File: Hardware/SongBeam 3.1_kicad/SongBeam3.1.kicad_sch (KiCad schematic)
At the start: 67 parts, among them IC1 ADAU7002ACBZ-R7, IC2 TXU0304PWR, IC3 TPS62842DGRR, IC4 TXU0304PWR, IC5 ADAU7002ACBZ-R7, IC6 LP5907MFX-1.8_NOPB, IC7 TEENSY_4.1, J1 Conn_01x02, J2 Conn_01x02, J3 Conn_01x04, J4 Conn_01x08, Q1 CPH6350-TL-W, Q2 AO6604, U1 TPL5110, U2 3034

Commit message: daughterBRD-UPDATE main BRD
added a full desing for daugther BRD, has a new microcontroller for 8 mics with TDM output
Start changes in the 4.0 version of the Soundbeam, making combatible with the daughter board
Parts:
- added C20, C21, C22: 22uF, Adafruit bq25185 Breakout:0805-NO, symbol Adafruit bq25185 Breakout-eagle-import:CAP_CERAMIC0805-NOOUTLINE
- added CHG0: ORANGE, Adafruit bq25185 Breakout:CHIPLED_0805_NOOUTLINE, symbol Adafruit bq25185 Breakout-eagle-import:LED0805_NOOUTLINE
- added D2 (x2): MBRX120, Adafruit bq25185 Breakout:SOD-123FL, symbol Adafruit bq25185 Breakout-eagle-import:DIODE-SCHOTTKYSOD-123FL
- added FAULT0: RED, Adafruit bq25185 Breakout:CHIPLED_0805_NOOUTLINE, symbol Adafruit bq25185 Breakout-eagle-import:LED0805_NOOUTLINE
- added IC8: BQ25185, Adafruit bq25185 Breakout:WSON10, symbol Adafruit bq25185 Breakout-eagle-import:BQ25185
- added JP2: HEADER-1X6OVALWAVE, Adafruit bq25185 Breakout:1X06_OVALWAVE, symbol Adafruit bq25185 Breakout-eagle-import:HEADER-1X6OVALWAVE
- added JP2, JP4: FIDUCIAL1.5X3, Adafruit bq25185 Breakout:FIDUCIAL_0.5MM, symbol Adafruit bq25185 Breakout-eagle-import:FIDUCIAL_0.5MM
- added JP7: HEADER-1X676MIL, Adafruit bq25185 Breakout:1X06_ROUND_76, symbol Adafruit bq25185 Breakout-eagle-import:HEADER-1X676MIL
- added R19, R21, R30: 5.1K, Adafruit bq25185 Breakout:0603-NO, symbol Adafruit bq25185 Breakout-eagle-import:RESISTOR_0603_NOOUT
- added R22, R23, R24: 1K, Adafruit bq25185 Breakout:0603-NO, symbol Adafruit bq25185 Breakout-eagle-import:RESISTOR_0603_NOOUT
- added R25, R31: 10K, Adafruit bq25185 Breakout:0603-NO, symbol Adafruit bq25185 Breakout-eagle-import:RESISTOR_0603_NOOUT
- added R26: 600, Adafruit bq25185 Breakout:0603-NO, symbol Adafruit bq25185 Breakout-eagle-import:RESISTOR_0603_NOOUT
- added R27: 300, Adafruit bq25185 Breakout:0603-NO, symbol Adafruit bq25185 Breakout-eagle-import:RESISTOR_0603_NOOUT
- added R28: 13K, Adafruit bq25185 Breakout:0603-NO, symbol Adafruit bq25185 Breakout-eagle-import:RESISTOR_0603_NOOUT
- added R29: 1200, Adafruit bq25185 Breakout:0603-NO, symbol Adafruit bq25185 Breakout-eagle-import:RESISTOR_0603_NOOUT
- added SJ1, SJ2, SJ3: SOLDERJUMPER_CLOSED, Adafruit bq25185 Breakout:SOLDERJUMPER_CLOSEDWIRE, symbol Adafruit bq25185 Breakout-eagle-import:SOLDERJUMPER_CLOSED
- added SJ4, SJ5, SJ6: SOLDERJUMPER, Adafruit bq25185 Breakout:SOLDERJUMPER_ARROW_NOPASTE, symbol Adafruit bq25185 Breakout-eagle-import:SOLDERJUMPER
- added U$11, U$16, U$18, U$19: MOUNTINGHOLE2.5, Adafruit bq25185 Breakout:MOUNTINGHOLE_2.5_PLATED, symbol Adafruit bq25185 Breakout-eagle-import:MOUNTINGHOLE2.5
- added VBAT0, VSYS0: JST2PH, Adafruit bq25185 Breakout:JSTPH2_BATT, symbol Adafruit bq25185 Breakout-eagle-import:CON_JST_PH_2PIN_MT_BATT
- added VSYSOK0: GREEN, Adafruit bq25185 Breakout:CHIPLED_0805_NOOUTLINE, symbol Adafruit bq25185 Breakout-eagle-import:LED0805_NOOUTLINE
- added X3: USBC, Adafruit bq25185 Breakout:USB_C_CUSB31-CFM2AX-01-X, symbol Adafruit bq25185 Breakout-eagle-import:USB_C
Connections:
- net GND: now also C20.2, C21.2, C22.2, IC8.5 (GND), IC8.PAD (GND), JP2.1, JP2.3, JP2.5, R19.1, R21.1, R22.2, R25.1, R26.2, R28.2, R31.1, SJ4.1, SJ5.1, SJ6.1, VBAT0.1, VBAT0.NC1 (P$1), VBAT0.NC2 (P$1), VSYS0.1, VSYS0.NC1 (P$1), VSYS0.NC2 (P$1), X3.A1B12 (GND), X3.B1A12 (GND)
- new net: R28.1, SJ2.1
- new net: D2.A, JP2.2
- new net: R22.1, VSYSOK0.C
- new net: R31.2, SJ1.1
- new net: CHG0.C, R23.2
- new net: R30.2, SJ6.2
- new net: FAULT0.C, R24.2
- new net: R19.2, X3.B5 (CC2)
- new net: R21.2, X3.A5 (CC1)
- new net: R27.2, SJ4.2
- new net: R26.1, SJ3.2
- new net: R29.2, SJ5.2
- new net: X3.A6 (D+), X3.B6 (D+)
- new net: X3.A7 (D-), X3.B7 (D-)
- new net /CE: IC8.4 (/CE), JP7.6, R25.2
- new net 5.0V: C21.1, CHG0.A, FAULT0.A, IC8.1 (VSYS), JP2.4, VSYS0.2, VSYSOK0.A
- new net ISET: IC8.8 (ISET), JP7.3, R27.1, R29.1, SJ3.1
- new net STAT1: IC8.9 (STAT1), JP7.4, R24.1
- new net STAT2: IC8.3 (STAT2), JP7.5, R23.1
- new net THERM: IC8.6 (TS/MR), JP7.1, SJ1.2
- new net USB: D2.A, X3.A4B9 (VBUS), X3.B4A9 (VBUS)
- new net VBAT: C22.1, IC8.2 (VBAT), JP2.6, VBAT0.2
- new net VBUS: C20.1, D2.C, D2.C, IC8.10 (VBUS)
- new net VSET: IC8.7 (VSET), JP7.2, R30.1, SJ2.2
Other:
- note added: "300Ω = 1000mA 600Ω = 500mA 1200Ω = 250mA"
- note added: "5.1KΩ = 3.65V / 1A 12KΩ = 4.2V / 1A"

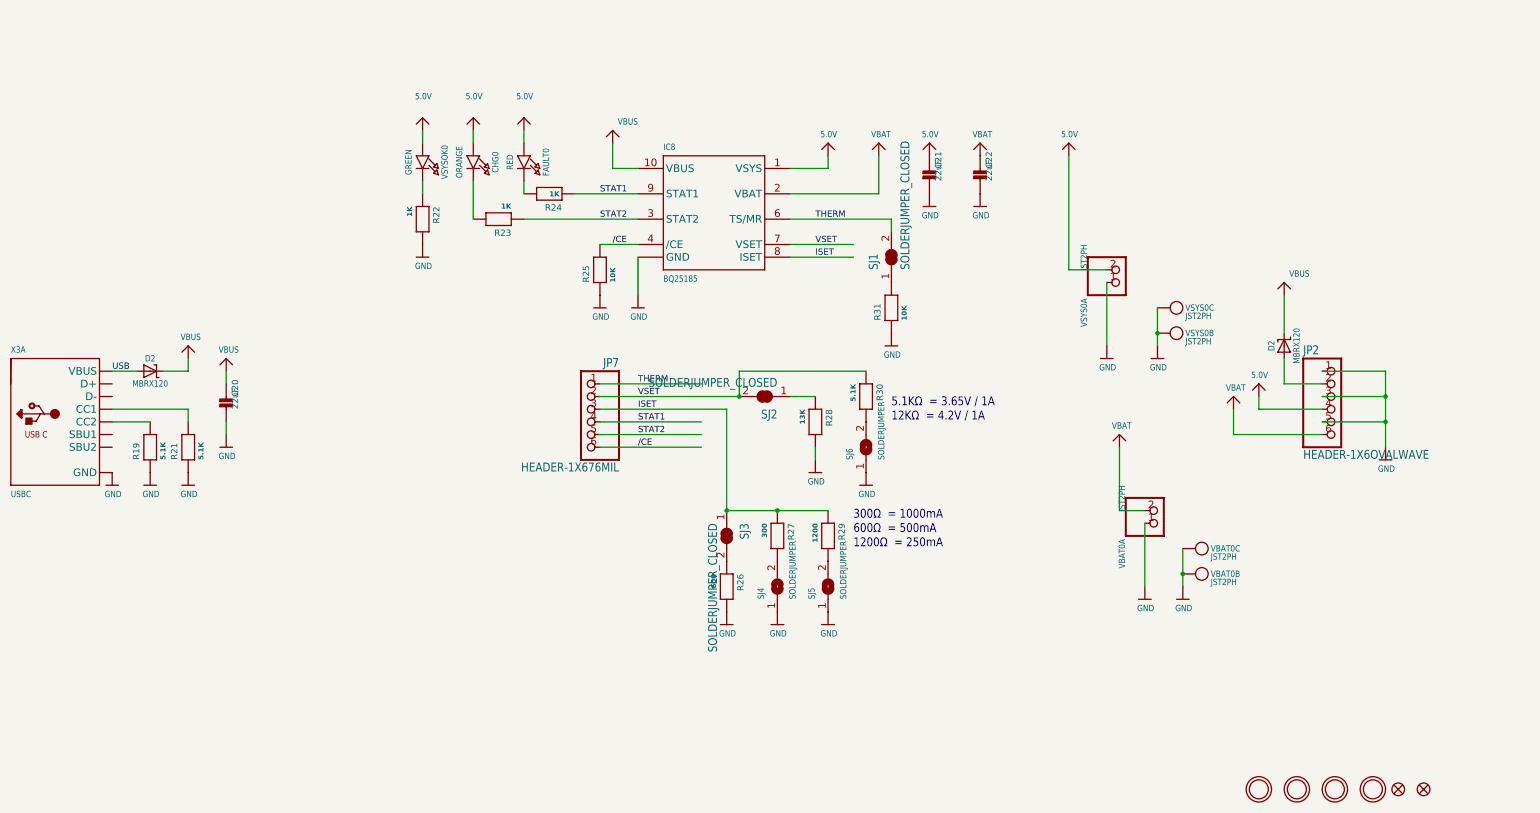
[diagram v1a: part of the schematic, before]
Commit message: tweaks in daugtherboard and develop in the main 4.0 board
changed voltage, added voltage translators and swiched from ethernet to HDMI
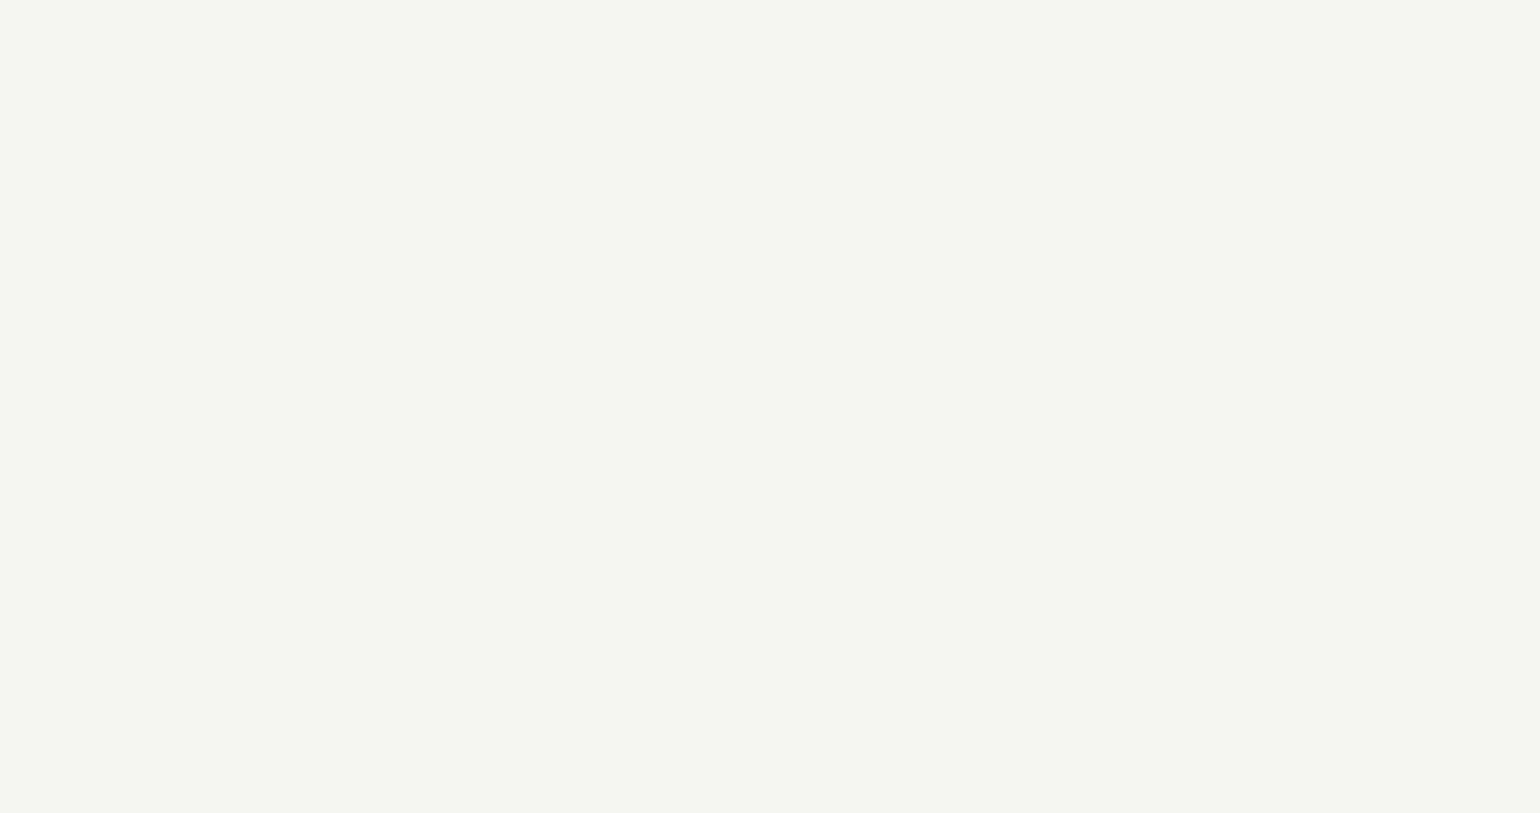
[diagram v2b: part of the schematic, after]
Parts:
- removed C20, C21, C22: 22uF, Adafruit bq25185 Breakout:0805-NO, symbol Adafruit bq25185 Breakout-eagle-import:CAP_CERAMIC0805-NOOUTLINE
- removed CHG0: ORANGE, Adafruit bq25185 Breakout:CHIPLED_0805_NOOUTLINE, symbol Adafruit bq25185 Breakout-eagle-import:LED0805_NOOUTLINE
- removed D2 (x2): MBRX120, Adafruit bq25185 Breakout:SOD-123FL, symbol Adafruit bq25185 Breakout-eagle-import:DIODE-SCHOTTKYSOD-123FL
- removed FAULT0: RED, Adafruit bq25185 Breakout:CHIPLED_0805_NOOUTLINE, symbol Adafruit bq25185 Breakout-eagle-import:LED0805_NOOUTLINE
- removed IC8: BQ25185, Adafruit bq25185 Breakout:WSON10, symbol Adafruit bq25185 Breakout-eagle-import:BQ25185
- removed JP2: HEADER-1X6OVALWAVE, Adafruit bq25185 Breakout:1X06_OVALWAVE, symbol Adafruit bq25185 Breakout-eagle-import:HEADER-1X6OVALWAVE
- removed JP2, JP4: FIDUCIAL1.5X3, Adafruit bq25185 Breakout:FIDUCIAL_0.5MM, symbol Adafruit bq25185 Breakout-eagle-import:FIDUCIAL_0.5MM
- removed JP7: HEADER-1X676MIL, Adafruit bq25185 Breakout:1X06_ROUND_76, symbol Adafruit bq25185 Breakout-eagle-import:HEADER-1X676MIL
- removed R19, R21, R30: 5.1K, Adafruit bq25185 Breakout:0603-NO, symbol Adafruit bq25185 Breakout-eagle-import:RESISTOR_0603_NOOUT
- removed R22, R23, R24: 1K, Adafruit bq25185 Breakout:0603-NO, symbol Adafruit bq25185 Breakout-eagle-import:RESISTOR_0603_NOOUT
- removed R25, R31: 10K, Adafruit bq25185 Breakout:0603-NO, symbol Adafruit bq25185 Breakout-eagle-import:RESISTOR_0603_NOOUT
- removed R26: 600, Adafruit bq25185 Breakout:0603-NO, symbol Adafruit bq25185 Breakout-eagle-import:RESISTOR_0603_NOOUT
- removed R27: 300, Adafruit bq25185 Breakout:0603-NO, symbol Adafruit bq25185 Breakout-eagle-import:RESISTOR_0603_NOOUT
- removed R28: 13K, Adafruit bq25185 Breakout:0603-NO, symbol Adafruit bq25185 Breakout-eagle-import:RESISTOR_0603_NOOUT
- removed R29: 1200, Adafruit bq25185 Breakout:0603-NO, symbol Adafruit bq25185 Breakout-eagle-import:RESISTOR_0603_NOOUT
- removed SJ1, SJ2, SJ3: SOLDERJUMPER_CLOSED, Adafruit bq25185 Breakout:SOLDERJUMPER_CLOSEDWIRE, symbol Adafruit bq25185 Breakout-eagle-import:SOLDERJUMPER_CLOSED
- removed SJ4, SJ5, SJ6: SOLDERJUMPER, Adafruit bq25185 Breakout:SOLDERJUMPER_ARROW_NOPASTE, symbol Adafruit bq25185 Breakout-eagle-import:SOLDERJUMPER
- removed U$11, U$16, U$18, U$19: MOUNTINGHOLE2.5, Adafruit bq25185 Breakout:MOUNTINGHOLE_2.5_PLATED, symbol Adafruit bq25185 Breakout-eagle-import:MOUNTINGHOLE2.5
- removed VBAT0, VSYS0: JST2PH, Adafruit bq25185 Breakout:JSTPH2_BATT, symbol Adafruit bq25185 Breakout-eagle-import:CON_JST_PH_2PIN_MT_BATT
- removed VSYSOK0: GREEN, Adafruit bq25185 Breakout:CHIPLED_0805_NOOUTLINE, symbol Adafruit bq25185 Breakout-eagle-import:LED0805_NOOUTLINE
- removed X3: USBC, Adafruit bq25185 Breakout:USB_C_CUSB31-CFM2AX-01-X, symbol Adafruit bq25185 Breakout-eagle-import:USB_C
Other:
- note removed: "300Ω = 1000mA 600Ω = 500mA 1200Ω = 250mA"
- note removed: "5.1KΩ = 3.65V / 1A 12KΩ = 4.2V / 1A"
